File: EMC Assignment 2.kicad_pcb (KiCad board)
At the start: 2 copper layers, 87 parts, among them IC1 LP2985AIM5-3.0_NOPB, J1 M40-3200445R, U1 LT8636, U2 ATMEGA16U2-MU, U3 ATMEGA328P-PU, U8 OPA4350EA_250, X2 USB, Y1 16MHz, Y2 16M

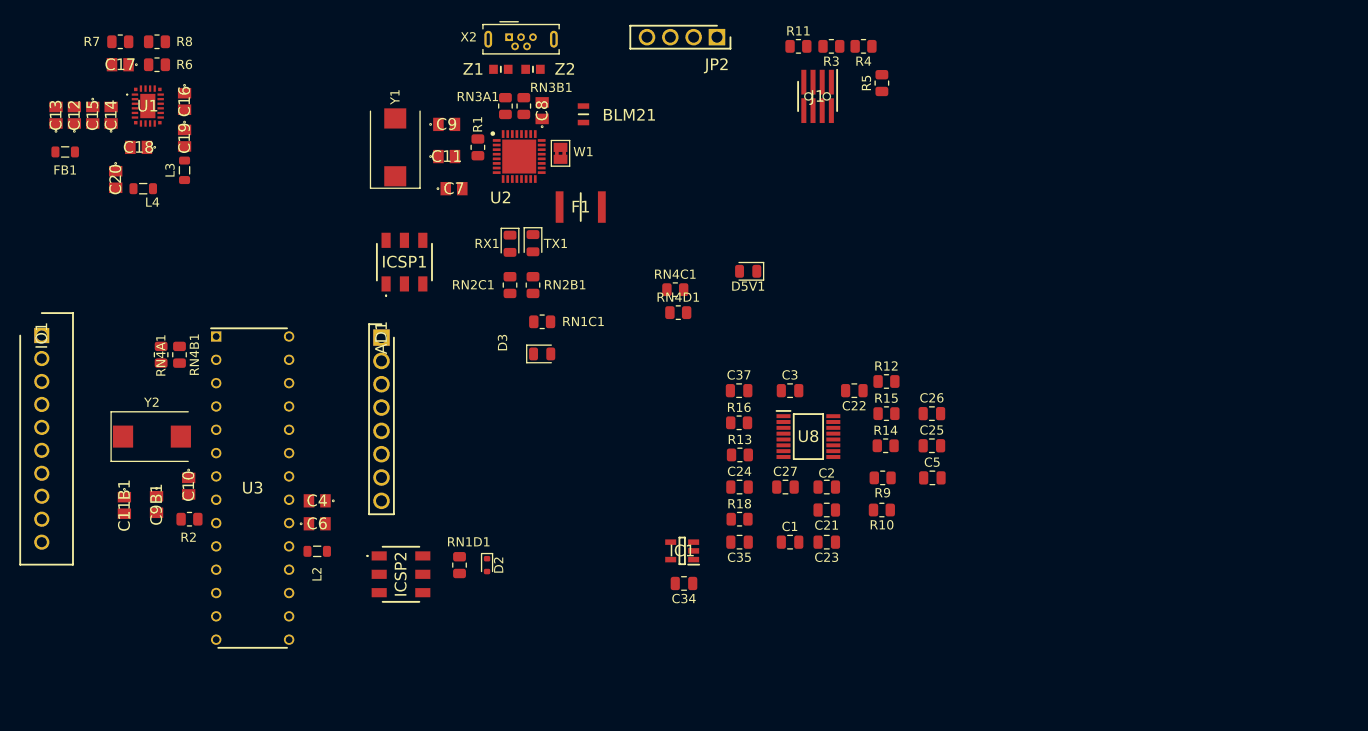
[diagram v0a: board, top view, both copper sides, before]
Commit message: more progress, much smaller board
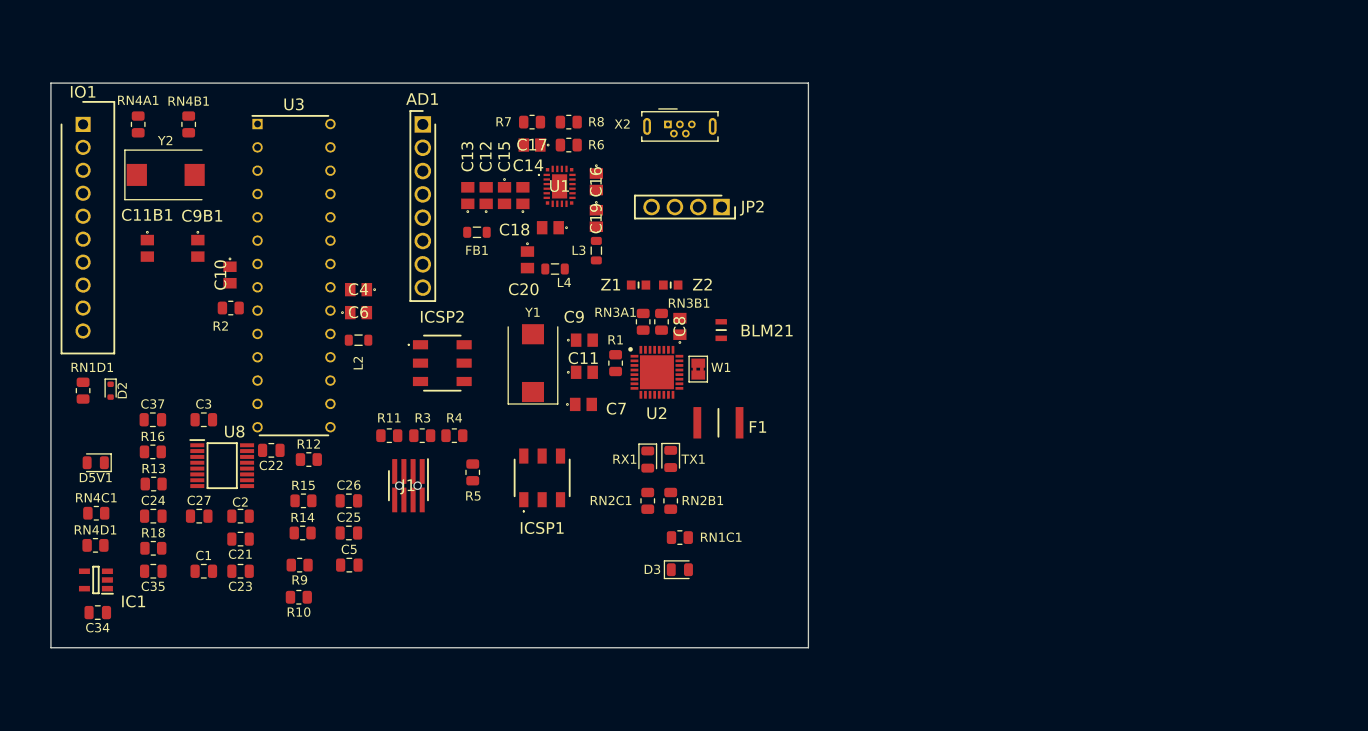
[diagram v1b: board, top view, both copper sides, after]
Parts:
- moved D5V1 74.1 mm to (20.4, 60.4)
- moved RN4D1 68.3 mm to (20.4, 69.3)
- moved RN4C1 67.6 mm to (20.4, 65.8)
- moved R9 64.2 mm to (42.6, 71.5)
- moved C25 64.2 mm to (48.0, 68.0)
- moved C26 64.2 mm to (48.0, 64.5)
- moved C5 64.2 mm to (48.0, 71.5)
- moved R10 64.2 mm to (42.5, 75.0)
- moved R14 64.2 mm to (42.9, 68.0)
- moved R15 64.2 mm to (43.0, 64.5)
- moved C1 63.9 mm to (32.1, 72.2)
- moved C2 63.9 mm to (36.1, 66.2)
- moved C21 63.9 mm to (36.1, 68.7)
- moved C23 63.9 mm to (36.1, 72.2)
- moved C24 63.9 mm to (26.6, 66.2)
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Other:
- board outline added: 82.5 x 61.5 mm

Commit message: COmmit before merge to main
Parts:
- moved Z1 14.2 mm to (81.8, 27.0)
- moved Z2 14.2 mm to (85.3, 27.0)
- moved JP2 11.0 mm to (96.0, 24.5), turned to -90 degrees
- moved X2 0.72 mm to (82.6, 22.8)
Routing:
- net /D-: track 0.00 -> 20.0 mm
- net /D+: track 0.00 -> 18.1 mm
- net Net-(U3-GND_2): track 0.00 -> 11.1 mm
- net /AD0: track 0.00 -> 10.1 mm
- net /AD2: track 0.00 -> 10.1 mm
- net /AD5: track 0.00 -> 10.1 mm
- net /AD4: track 0.00 -> 10.1 mm
- net /AD3: track 0.00 -> 10.1 mm
- net /AD1: track 0.00 -> 10.1 mm
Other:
- copper layers 2 -> 4

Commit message: WIP, pretty good point
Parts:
- C10, C11, C11B1, C12, C13, C14, C15, C16, C17, C18, C19, C20, C4, C6, C7, C8, C9, C9B1: footprint emc:C0805 -> Capacitor_SMD:C_0805_2012Metric
- moved C23 86.0 mm to (113.5, 34.5), turned to 90 degrees
- moved C21 81.1 mm to (112.5, 41.2), turned to 0 degrees
- moved C35 77.8 mm to (94.2, 33.7), turned to 90 degrees
- moved C22 77.1 mm to (111.2, 30.8), turned to 90 degrees
- moved R10 76.7 mm to (112.6, 43.8)
- moved C37 74.4 mm to (96.5, 30.2), turned to 90 degrees
- moved R16 74.4 mm to (96.5, 33.7), turned to -90 degrees
- moved R9 72.9 mm to (109.0, 41.2)
- moved R12 72.3 mm to (111.2, 34.5), turned to -90 degrees
- moved R15 72.1 mm to (108.5, 34.5), turned to -90 degrees
- moved R14 69.7 mm to (109.1, 46.0), turned to 180 degrees
- moved U8 69.6 mm to (100.4, 39.2)
- moved C26 69.3 mm to (108.5, 30.7), turned to 90 degrees
- moved IC1 68.6 mm to (87.8, 60.4), turned to 0 degrees
- moved C34 68.6 mm to (88.3, 65.9), turned to 90 degrees
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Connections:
- C24 pad 2: Net-(U8--V) -> GND
- C25 pad 2: Net-(U8--V) -> GND
- C26 pad 2: Net-(U8--V) -> GND
- C37 pad 2: Net-(U8--V) -> GND
- U8 pad 13: Net-(U8--V) -> GND
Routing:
- net GND: track 0.00 -> 69.8 mm, vias 0 -> 10
- net +5V: track 0.00 -> 46.4 mm, vias 0 -> 6
- net /UGND: track 0.00 -> 43.8 mm
- net /RESET: track 0.00 -> 43.2 mm, vias 0 -> 2
- net /PB4: track 0.00 -> 35.9 mm
- net Net-(U3-PB6_(PCINT6/XTAL1/TOSC1)): track 0.00 -> 33.6 mm, vias 0 -> 2
- net /AREF: track 0.00 -> 31.7 mm, vias 0 -> 2
- net Net-(U3-PB7_(PCINT7/XTAL2/TOSC2)): track 0.00 -> 30.6 mm
- net /PB5: track 0.00 -> 25.2 mm
- net Net-(U3-AVCC): track 0.00 -> 25.0 mm
- net /RESET2: track 0.00 -> 24.6 mm, vias 0 -> 2
- net /PB6: track 0.00 -> 21.6 mm
- net /D-: track 20.0 -> 0.33 mm
- net Net-(C13-Pad1): track 0.00 -> 18.6 mm
- net /INTVCE: track 0.00 -> 18.4 mm, vias 0 -> 2
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- added copper zone on In2.Cu, net +5V
- added copper zone on In1.Cu, net GND
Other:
- board outline removed

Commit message: Pre reannotate test
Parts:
- moved R18 10.7 mm to (91.8, 30.2), turned to -90 degrees
- moved C27 5.64 mm to (91.8, 34.0), turned to 90 degrees
- moved C22 3.28 mm to (108.0, 30.3)
- moved C23 3.28 mm to (110.2, 34.1)
- moved R11 3.28 mm to (110.2, 30.3)
- moved R12 3.28 mm to (108.0, 34.1)
- moved R15 3.28 mm to (105.2, 34.0)
- moved C26 3.28 mm to (105.2, 30.3)
- moved C2 3.09 mm to (92.2, 40.0)
- moved C24 3.09 mm to (88.4, 44.5)
- moved C3 3.09 mm to (92.2, 42.2)
- moved R13 3.09 mm to (92.2, 44.5)
- moved R3 3.09 mm to (88.5, 42.2)
- moved R4 3.09 mm to (88.5, 40.0)

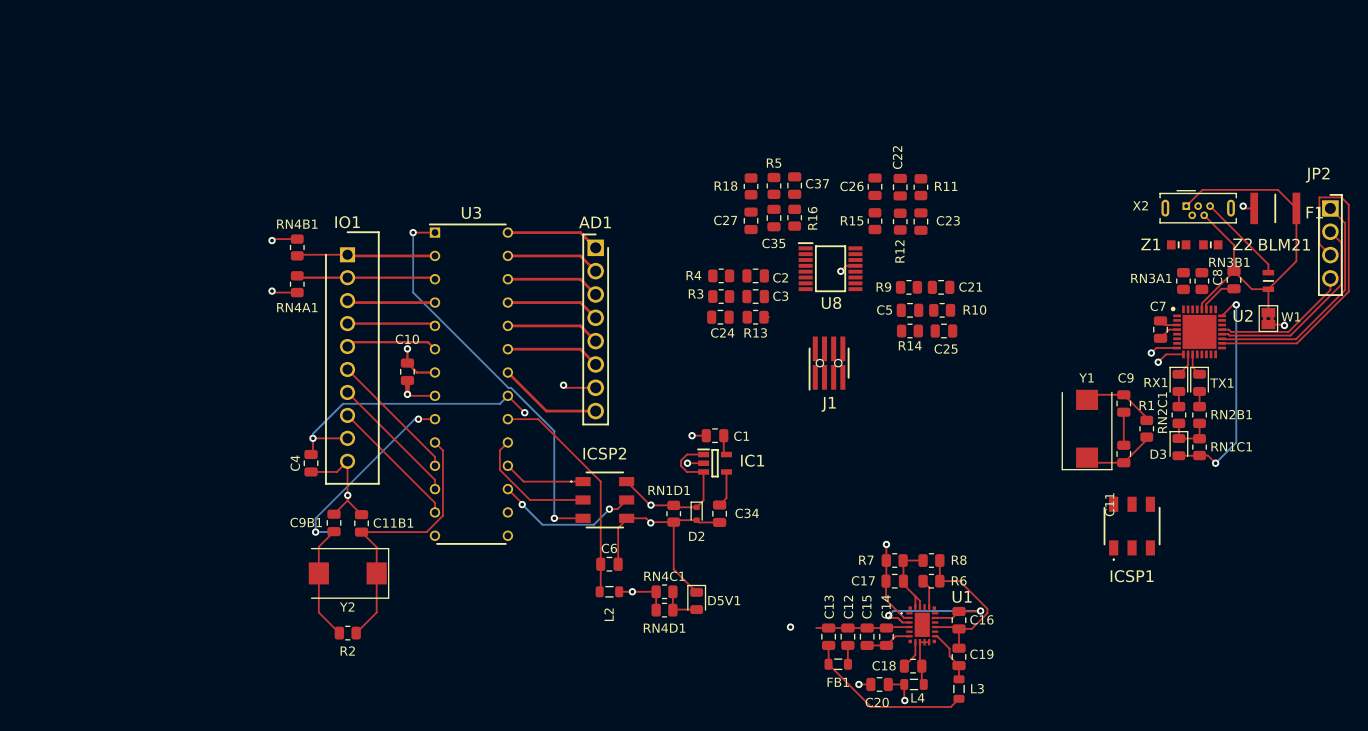
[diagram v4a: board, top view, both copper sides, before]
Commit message: Almost all routing done
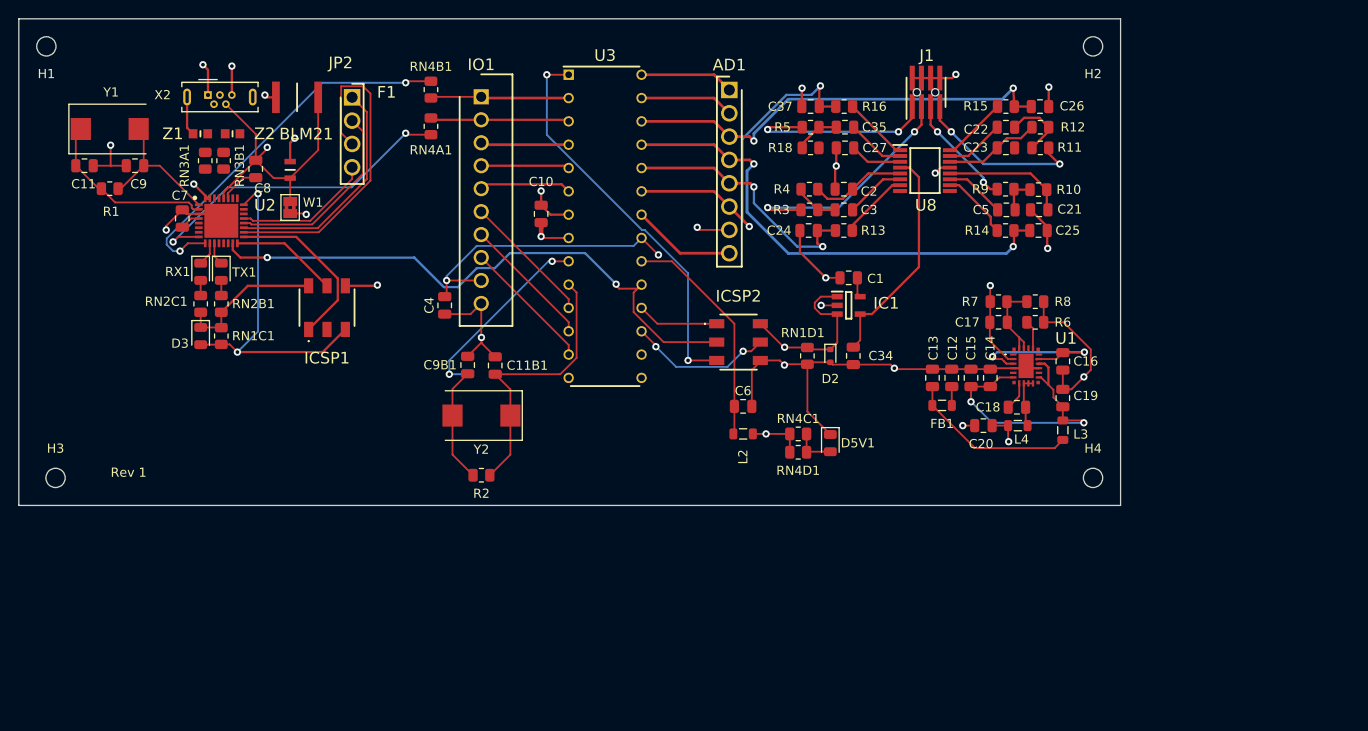
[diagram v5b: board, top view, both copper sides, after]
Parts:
- added H1: MountingHole_Pad, MountingHole:MountingHole_2.1mm, F.Cu at (15.0, 15.0)
- added H2: MountingHole_Pad, MountingHole:MountingHole_2.1mm, F.Cu at (129.0, 15.0)
- added H3: MountingHole_Pad, MountingHole:MountingHole_2.1mm, F.Cu at (16.0, 62.0)
- added H4: MountingHole_Pad, MountingHole:MountingHole_2.1mm, F.Cu at (129.0, 62.0)
- moved C11 117.5 mm to (19.2, 28.0), turned to 180 degrees
- moved R1 115.9 mm to (21.9, 30.5), turned to 180 degrees
- moved Y1 111.3 mm to (21.9, 24.0), turned to 0 degrees
- moved C9 110.8 mm to (24.7, 28.0), turned to 0 degrees
- moved RN3A1 107.3 mm to (32.3, 27.5)
- moved RN3B1 107.3 mm to (34.3, 27.5)
- moved X2 107.2 mm to (32.6, 20.3)
- moved BLM21 107.2 mm to (41.6, 28.4)
- moved C7 107.2 mm to (29.8, 33.8)
- moved C8 107.2 mm to (37.8, 28.4)
- moved D3 107.2 mm to (31.8, 46.5)
- moved F1 107.2 mm to (42.3, 20.6)
- moved JP2 107.2 mm to (48.3, 20.6)
- moved RN1C1 107.2 mm to (34.1, 46.5)
- moved RN2B1 107.2 mm to (34.1, 43.0)
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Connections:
- BLM21 pad 2: Net-(X2-GND) -> GND
- C16 pad 2: Net-(U1-GND_2) -> GND
- C19 pad 1: Net-(U1-GND_2) -> GND
- R6 pad 2: Net-(U1-GND_2) -> GND
- R8 pad 2: Net-(U1-GND_2) -> GND
- U1 pad 13: Net-(U1-GND_2) -> GND
- U1 pad 21: Net-(U1-GND_2) -> GND
- X2 pad 5: Net-(X2-GND) -> GND
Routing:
- net GND: track 69.8 -> 139.9 mm, vias 10 -> 21
- net /SCK: track 13.8 -> 64.0 mm, vias 0 -> 2
- net /AD2: track 10.2 -> 53.3 mm, vias 0 -> 2
- net /AD3: track 10.2 -> 48.2 mm, vias 0 -> 2
- net /M8RXD: track 5.92 -> 41.4 mm
- net /M8TXD: track 5.85 -> 36.1 mm
- net /AD0: track 10.2 -> 38.4 mm, vias 0 -> 2
- net /ADCB: track 0.00 -> 26.2 mm, vias 0 -> 2
- net /ADCA: track 0.00 -> 21.6 mm, vias 0 -> 2
- net +3.3V: track 3.91 -> 24.7 mm
- net /VIN: track 10.9 -> 31.5 mm, vias 0 -> 2
- net /MISO2: track 0.00 -> 19.0 mm
- net /ADCD: track 0.00 -> 18.8 mm, vias 0 -> 2
- net /AD1: track 10.2 -> 28.6 mm, vias 0 -> 2
- net Net-(U1-GND_2): track 17.8 -> 0.00 mm
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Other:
- board outline added: 120 x 53 mm
- board text added: "Rev 1"
